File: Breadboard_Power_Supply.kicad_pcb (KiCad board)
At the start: 2 copper layers, 30 x 60 mm, 22 parts, among them J1 9V Battery, J2 USB_B, J3 Barrel_Jack_Switch, J4 1, J5 2, J6 3, SW1 SW_DIP_x03, U1 AMS1117-5.0, U2 AMS1117-3.3

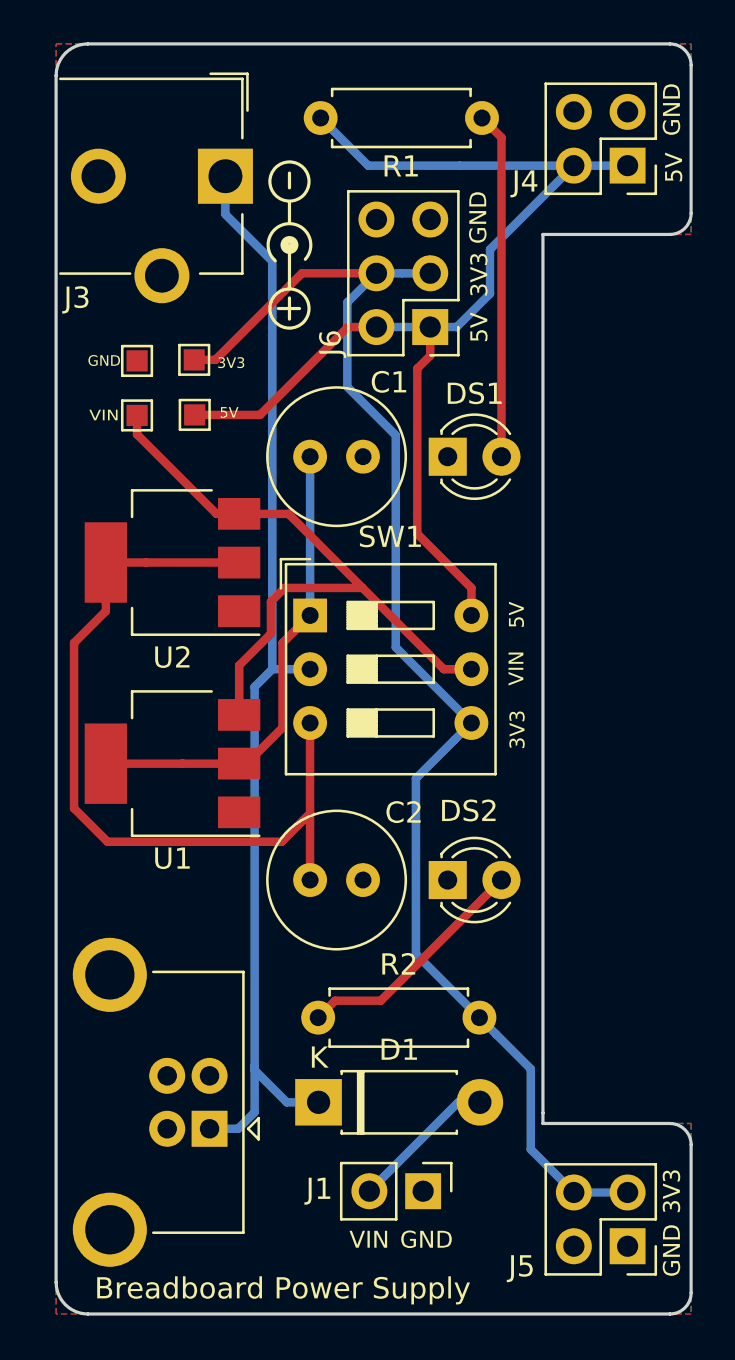
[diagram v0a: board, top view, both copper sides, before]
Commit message: Changed most footprints to SMD + Variable voltage
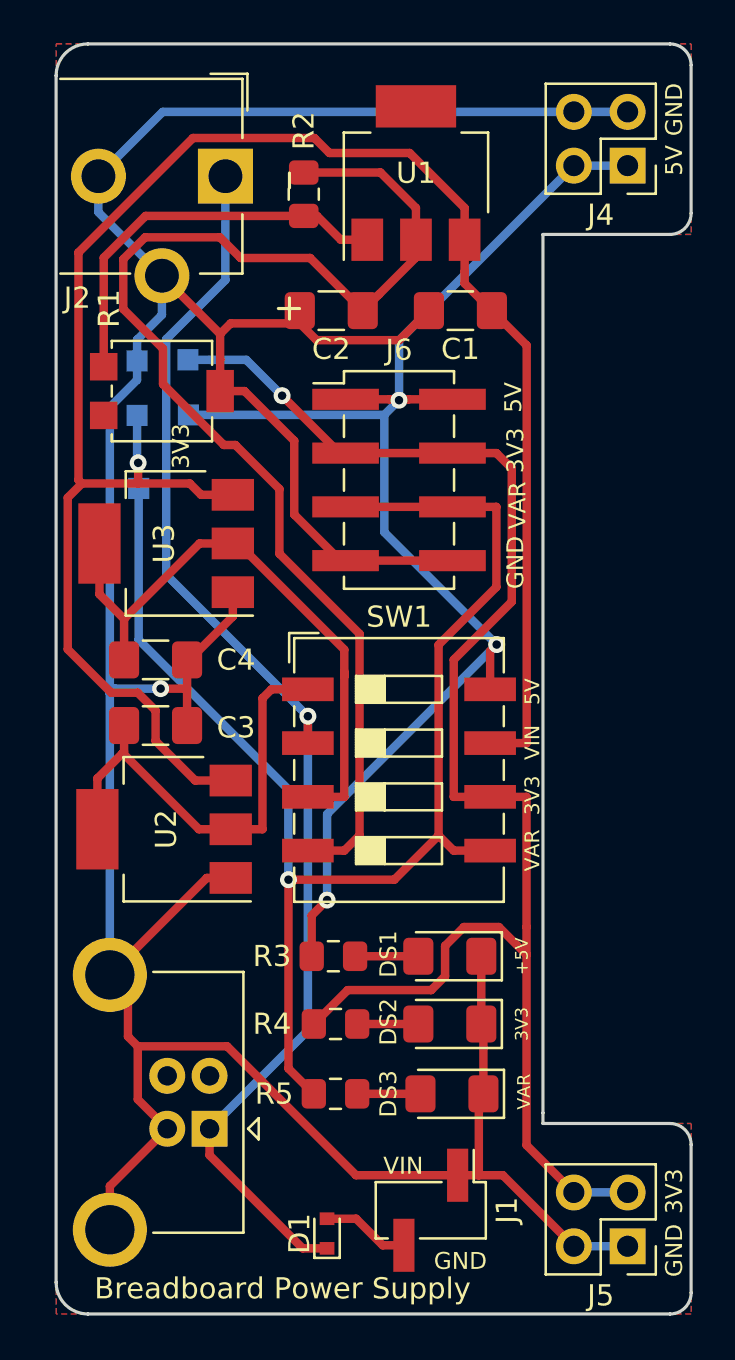
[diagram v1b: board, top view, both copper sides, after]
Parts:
- removed Polarity: Symbol_Barrel_Polarity, Symbol:Symbol_Barrel_Polarity
- removed REF**: OSHW-Logo2_7.3x6mm_SilkScreen, Symbol:OSHW-Logo2_7.3x6mm_SilkScreen
- added C1: 0.1uF, Capacitor_SMD:C_1206_3216Metric_Pad1.42x1.75mm_HandSolder, F.Cu at (151.6, 72.1)
- added C2: 1uF, Capacitor_SMD:C_1206_3216Metric_Pad1.42x1.75mm_HandSolder, F.Cu at (145.5, 72.1)
- added DS3: LED, LED_SMD:LED_1206_3216Metric_Pad1.42x1.75mm_HandSolder, F.Cu at (151.2, 109.1)
- added R1: 5k, Potentiometer_SMD:Potentiometer_Bourns_3314G_Vertical, F.Cu at (137.5, 75.9)
- added R2: 240R, Resistor_SMD:R_0805_2012Metric_Pad1.15x1.40mm_HandSolder, F.Cu at (144.2, 66.6)
- added R5: 820R, Resistor_SMD:R_0805_2012Metric_Pad1.15x1.40mm_HandSolder, F.Cu at (145.7, 109.1)
- added TP5: TestPoint, TestPoint:TestPoint_Pad_1.0x1.0mm, B.Cu at (136.4, 80.5)
- added U1: LM317_3PinPackage, Package_TO_SOT_SMD:SOT-223, F.Cu at (149.5, 65.6)
- C3: renamed from C1; footprint Capacitor_THT:C_Radial_D6.3mm_H11.0mm_P2.50mm -> Capacitor_SMD:C_1206_3216Metric_Pad1.42x1.75mm_HandSolder
- C4: renamed from C2; footprint Capacitor_THT:C_Radial_D6.3mm_H11.0mm_P2.50mm -> Capacitor_SMD:C_1206_3216Metric_Pad1.42x1.75mm_HandSolder
- D1: value 1N4007 -> 1N4148WT; footprint Diode_THT:D_DO-41_SOD81_P7.62mm_Horizontal -> Diode_SMD:D_SOD-523
- DS1, DS2: footprint LED_THT:LED_D3.0mm -> LED_SMD:LED_1206_3216Metric_Pad1.42x1.75mm_HandSolder
- J1: footprint Connector_PinHeader_2.54mm:PinHeader_1x02_P2.54mm_Vertical -> Connector_PinHeader_2.54mm:PinHeader_1x02_P2.54mm_Vertical_SMD_Pin1Left
- J6: value 3 -> Conn_02x04_Odd_Even; footprint Connector_PinHeader_2.54mm:PinHeader_2x03_P2.54mm_Vertical -> Connector_PinHeader_2.54mm:PinHeader_2x04_P2.54mm_Vertical_SMD
- R3: renamed from R1; footprint Resistor_THT:R_Axial_DIN0207_L6.3mm_D2.5mm_P7.62mm_Horizontal -> Resistor_SMD:R_0805_2012Metric_Pad1.15x1.40mm_HandSolder
- R4: renamed from R2; footprint Resistor_THT:R_Axial_DIN0207_L6.3mm_D2.5mm_P7.62mm_Horizontal -> Resistor_SMD:R_0805_2012Metric_Pad1.15x1.40mm_HandSolder
- SW1: value SW_DIP_x03 -> SW_DIP_x04; footprint Button_Switch_THT:SW_DIP_SPSTx03_Slide_9.78x9.8mm_W7.62mm_P2.54mm -> Button_Switch_SMD:SW_DIP_SPSTx04_Slide_9.78x12.34mm_W8.61mm_P2.54mm
- TP1: renamed from VIN; moved to B.Cu
- TP2: renamed from GND; moved to B.Cu
- TP3: renamed from  5V; moved to B.Cu
- TP4: renamed from 3V3; moved to B.Cu
- moved R3 39.6 mm to (145.6, 102.6)
- moved DS1 23.6 mm to (151.1, 102.6), turned to 180 degrees
- moved C3 14.6 mm to (137.2, 91.7)
- moved C4 12.7 mm to (137.2, 88.6)
- moved SW1 8.42 mm to (148.7, 93.8)
- moved J6 7.37 mm to (148.7, 80.1), turned to 0 degrees
- moved R4 6.81 mm to (145.7, 105.8), turned to 0 degrees
- moved DS2 6.80 mm to (151.1, 105.8), turned to 180 degrees
- moved D1 6.21 mm to (145.3, 115.7), turned to 90 degrees
- moved U2 3.13 mm to (137.6, 96.6)
- moved J1 0.97 mm to (150.2, 114.6)
- moved U3 0.95 mm to (137.7, 83.1)
- moved TP3 0.30 mm to (138.8, 77.0)
- moved TP4 0.30 mm to (138.7, 74.4)
- renumbered J3 to J2, J2 to J3, U1 to U2, U2 to U3
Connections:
- net 3.3V_OUT renamed /3.3V_OUT
- net 5V_OUT renamed /5V_OUT
- J3 pad 2: Net-(J2-Pad2) -> (no net)
- J3 pad 3: Net-(J2-Pad3) -> (no net)
- J3 pad 4: Net-(J2-Pad4) -> GND
- J6 pad 5: GND -> /VAR_VLG
- J6 pad 6: GND -> /VAR_VLG
- SW1 pad 4: +3V3 -> /VAR_VLG_OUT
- SW1 pad 5: VIN -> /VAR_VLG
- SW1 pad 6: +5V -> +3V3
- TP1 pad 1: VIN -> /VIN
- U2 pad 3: VIN -> /VIN
- U3 pad 3: VIN -> /VIN
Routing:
- net GND: track 0.00 -> 171.7 mm, vias 0 -> 1
- net /VIN: track 0.00 -> 90.9 mm, vias 0 -> 1
- net /VAR_VLG: track 0.00 -> 66.5 mm, vias 0 -> 1
- net /VAR_VLG_OUT: track 0.00 -> 60.0 mm
- net VIN: track 31.9 -> 0.00 mm
- net Net-(R1-Pad1): track 0.00 -> 18.9 mm
- net Net-(DS1-Pad2): track 16.4 -> 2.99 mm
- net +5V: track 54.4 -> 66.0 mm, vias 0 -> 3
- net /3.3V_OUT: track 40.2 -> 28.9 mm
- net Net-(DS2-Pad2): track 11.4 -> 2.89 mm
- net VDC: track 53.5 -> 60.7 mm, vias 0 -> 1
- net +3V3: track 66.0 -> 73.0 mm, vias 0 -> 1
- net Net-(DS3-Pad2): track 0.00 -> 2.99 mm
- net Net-(D1-Pad2): track 6.96 -> 4.15 mm
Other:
- net class Default: clearance 0.3 -> 0.1
- rule trace_clearance: 0.3 -> 0.1
- board text added: "+5V"
- board text added: "VAR"
- board text added: "VIN switch in the middle for simultaneous switching"

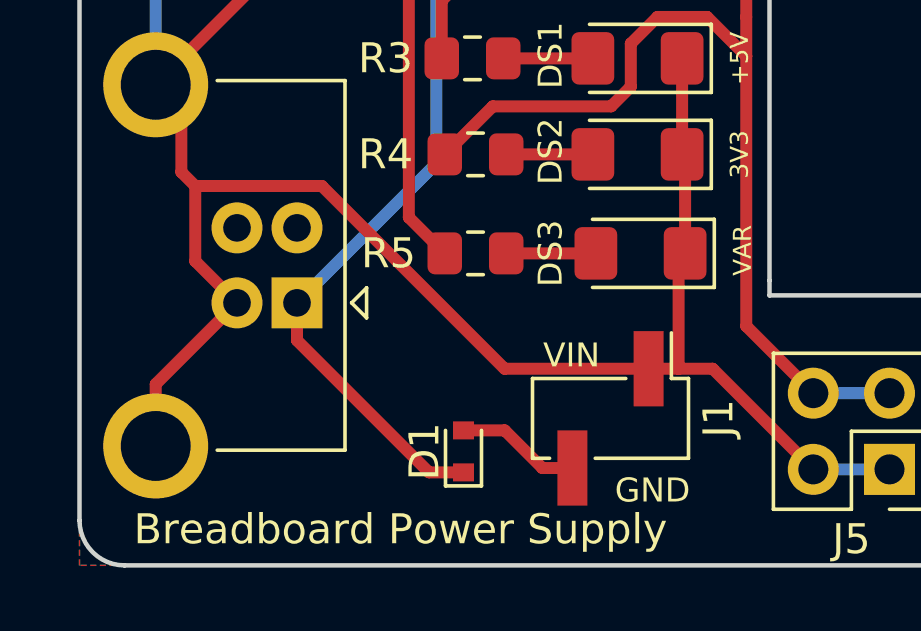
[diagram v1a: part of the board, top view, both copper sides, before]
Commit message: Protection diode changed + Datasheets
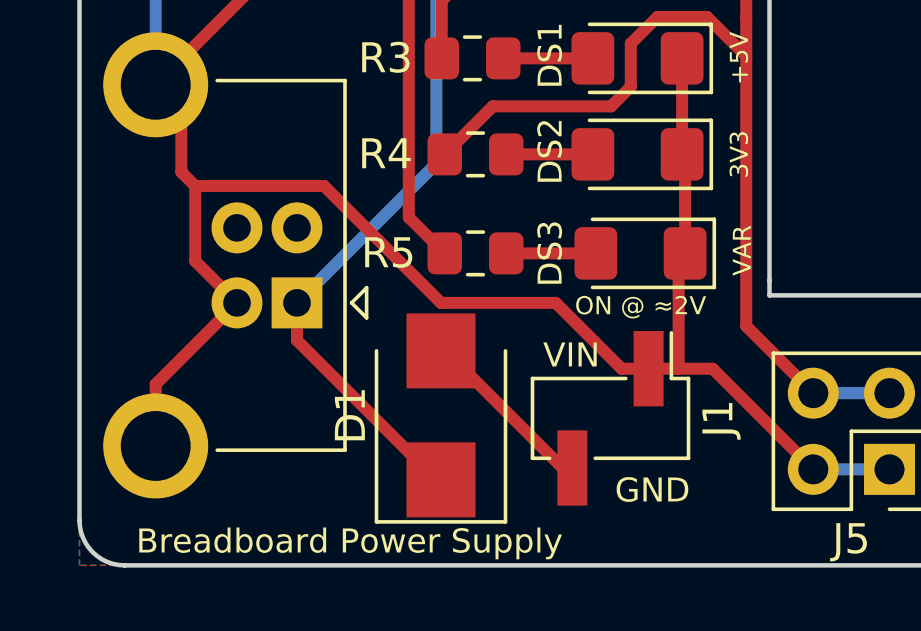
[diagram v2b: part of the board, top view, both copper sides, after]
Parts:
- D1: value 1N4148WT -> SS22T3G; footprint Diode_SMD:D_SOD-523 -> Diode_SMD:D_SMB
- moved D1 1.42 mm to (144.6, 114.5)
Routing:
- net Net-(D1-Pad2): track 4.15 -> 6.09 mm
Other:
- board text added: "ON @ ≈2V"
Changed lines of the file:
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@@
   (general
     (thickness 1.6)
-    (drawings 54)
-    (tracks 219)
+    (drawings 55)
+    (tracks 221)
     (zones 0)
     (modules 28)
@@
     (add_net "Net-(R1-Pad1)")
     (add_net VDC)
+  )
+  (module Diode_SMD:D_SMB (layer F.Cu)
+    (at 144.55 114.5 90)
+    (descr "Diode SMB (DO-214AA)")
+    (tags "Diode SMB (DO-214AA)")
+    (attr smd)
+    (fp_text reference D1 (at 0 -3 90) (layer F.SilkS)
+      (effects (font (size 1 1) (thickness 0.15)))
+    )
+    (fp_text value SS22T3G (at 0 3.1 90) (layer F.Fab)
+      (effects (font (size 1 1) (thickness 0.15)))
+    )
+    (fp_line (start -3.55 -2.15) (end 2.15 -2.15) (layer F.SilkS) (width 0.12))
+    (fp_line (start -3.55 2.15) (end 2.15 2.15) (layer F.SilkS) (width 0.12))
+    (fp_line (start -0.64944 0.00102) (end 0.50118 -0.79908) (layer F.Fab) (width 0.1))
+    (fp_line (start -0.64944 0.00102) (end 0.50118 0.75032) (layer F.Fab) (width 0.1))
+    (fp_line (start 0.50118 0.75032) (end 0.50118 -0.79908) (layer F.Fab) (width 0.1))
+    (fp_line (start -0.64944 -0.79908) (end -0.64944 0.80112) (layer F.Fab) (width 0.1))
+    (fp_line (start 0.50118 0.00102) (end 1.4994 0.00102) (layer F.Fab) (width 0.1))
+    (fp_line (start -0.64944 0.00102) (end -1.55114 0.00102) (layer F.Fab) (width 0.1))
+    (fp_line (start -3.65 2.25) (end -3.65 -2.25) (layer F.CrtYd) (width 0.05))
+    (fp_line (start 3.65 2.25) (end -3.65 2.25) (layer F.CrtYd) (width 0.05))
+    (fp_line (start 3.65 -2.25) (end 3.65 2.25) (layer F.CrtYd) (width 0.05))
+    (fp_line (start -3.65 -2.25) (end 3.65 -2.25) (layer F.CrtYd) (width 0.05))
+    (fp_line (start 2.3 -2) (end -2.3 -2) (layer F.Fab) (width 0.1))
+    (fp_line (start 2.3 -2) (end 2.3 2) (layer F.Fab) (width 0.1))
+    (fp_line (start -2.3 2) (end -2.3 -2) (layer F.Fab) (width 0.1))
+    (fp_line (start 2.3 2) (end -2.3 2) (layer F.Fab) (width 0.1))
+    (fp_line (start -3.55 -2.15) (end -3.55 2.15) (layer F.SilkS) (width 0.12))
+    (fp_text user %R (at 0 -3 90) (layer F.Fab)
+      (effects (font (size 1 1) (thickness 0.15)))
+    )
+    (pad 2 smd rect (at 2.15 0 90) (size 2.5 2.3) (layers F.Cu F.Paste F.Mask)
+      (net 7 "Net-(D1-Pad2)"))
+    (pad 1 smd rect (at -2.15 0 90) (size 2.5 2.3) (layers F.Cu F.Paste F.Mask)
+      (net 2 VDC))
+    (model ${KISYS3DMOD}/Diode_SMD.3dshapes/D_SMB.wrl
+      (at (xyz 0 0 0))
+      (scale (xyz 1 1 1))
+      (rotate (xyz 0 0 0))
+    )
   )
   (module Potentiometer_SMD:Potentiometer_Bourns_3314G_Vertical (layer F.Cu)
@@
     )
   )
-  (module Diode_SMD:D_SOD-523 (layer F.Cu)
-    (at 145.3 115.7 90)
-    (descr "http://www.diodes.com/datasheets/ap02001.pdf p.144")
-    (tags "Diode SOD523")
-    (attr smd)
-    (fp_text reference D1 (at 0 -1.3 90) (layer F.SilkS)
-      (effects (font (size 1 1) (thickness 0.15)))
-    )
-    (fp_text value 1N4148WT (at 0 1.4 90) (layer F.Fab)
-      (effects (font (size 1 1) (thickness 0.15)))
-    )
-    (fp_line (start 0.7 0.6) (end -1.15 0.6) (layer F.SilkS) (width 0.12))
-    (fp_line (start 0.7 -0.6) (end -1.15 -0.6) (layer F.SilkS) (width 0.12))
-    (fp_line (start 0.65 0.45) (end -0.65 0.45) (layer F.Fab) (width 0.1))
-    (fp_line (start -0.65 0.45) (end -0.65 -0.45) (layer F.Fab) (width 0.1))
-    (fp_line (start -0.65 -0.45) (end 0.65 -0.45) (layer F.Fab) (width 0.1))
-    (fp_line (start 0.65 -0.45) (end 0.65 0.45) (layer F.Fab) (width 0.1))
-    (fp_line (start -0.2 0.2) (end -0.2 -0.2) (layer F.Fab) (width 0.1))
-    (fp_line (start -0.2 0) (end -0.35 0) (layer F.Fab) (width 0.1))
-    (fp_line (start -0.2 0) (end 0.1 0.2) (layer F.Fab) (width 0.1))
-    (fp_line (start 0.1 0.2) (end 0.1 -0.2) (layer F.Fab) (width 0.1))
-    (fp_line (start 0.1 -0.2) (end -0.2 0) (layer F.Fab) (width 0.1))
-    (fp_line (start 0.1 0) (end 0.25 0) (layer F.Fab) (width 0.1))
-    (fp_line (start 1.25 0.7) (end -1.25 0.7) (layer F.CrtYd) (width 0.05))
-    (fp_line (start -1.25 0.7) (end -1.25 -0.7) (layer F.CrtYd) (width 0.05))
-    (fp_line (start -1.25 -0.7) (end 1.25 -0.7) (layer F.CrtYd) (width 0.05))
-    (fp_line (start 1.25 -0.7) (end 1.25 0.7) (layer F.CrtYd) (width 0.05))
-    (fp_line (start -1.15 -0.6) (end -1.15 0.6) (layer F.SilkS) (width 0.12))
-    (fp_text user %R (at 0 -1.3 90) (layer F.Fab)
-      (effects (font (size 1 1) (thickness 0.15)))
-    )
-    (pad 1 smd rect (at -0.7 0 270) (size 0.6 0.7) (layers F.Cu F.Paste F.Mask)
-      (net 2 VDC))
-    (pad 2 smd rect (at 0.7 0 270) (size 0.6 0.7) (layers F.Cu F.Paste F.Mask)
-      (net 7 "Net-(D1-Pad2)"))
-    (model ${KISYS3DMOD}/Diode_SMD.3dshapes/D_SOD-523.wrl
-      (at (xyz 0 0 0))
-      (scale (xyz 1 1 1))
-      (rotate (xyz 0 0 0))
-    )
-  )
   (module Capacitor_SMD:C_1206_3216Metric_Pad1.42x1.75mm_HandSolder (layer F.Cu)
     (at 137.2 88.6)
@@
     )
   )
+  (gr_text "ON @ ≈2V" (at 151.2 110.85) (layer F.SilkS)
+    (effects (font (size 0.6 0.6) (thickness 0.08)))
+  )
+  (gr_text "Breadboard Power Supply" (at 141.5 118.7) (layer F.SilkS)
+    (effects (font (size 0.8 0.8) (thickness 0.1)))
+  )
   (gr_text "VIN switch in the middle for simultaneous switching" (at 157.7 89.8 90) (layer Cmts.User)
     (effects (font (size 0.9 0.9) (thickness 0.1)))
@@
   (gr_text GND (at 151.6 117) (layer F.SilkS)
     (effects (font (size 0.8 0.8) (thickness 0.15)))
-  )
-  (gr_text "Breadboard Power Supply" (at 143.2 118.3) (layer F.SilkS)
-    (effects (font (size 1 1) (thickness 0.25)))
   )
   (gr_line (start 161 91) (end 161 115) (layer Dwgs.User) (width 0.15))
@@
   (segment (start 152.4703 112.945) (end 152.4703 109.3172) (width 0.4) (layer F.Cu) (net 1))
   (segment (start 152.4703 109.3172) (end 152.6875 109.1) (width 0.4) (layer F.Cu) (net 1))
-  (segment (start 136.3587 106.8542) (end 140.5798 106.8542) (width 0.4) (layer F.Cu) (net 1))
-  (segment (start 140.5798 106.8542) (end 146.6706 112.945) (width 0.4) (layer F.Cu) (net 1))
-  (segment (start 146.6706 112.945) (end 151.47 112.945) (width 0.4) (layer F.Cu) (net 1))
   (segment (start 136.325 74.475) (end 136.325 73.4747) (width 0.4) (layer B.Cu) (net 1))
   (segment (start 138.6875 91.7) (end 138.6875 89.958) (width 0.4) (layer F.Cu) (net 1))
@@
   (segment (start 135.04 76.66) (end 136.325 75.375) (width 0.4) (layer B.Cu) (net 1))
   (segment (start 135.04 90.2006) (end 135.04 76.66) (width 0.4) (layer B.Cu) (net 1))
+  (segment (start 150.57 112.945) (end 151.47 112.945) (width 0.4) (layer F.Cu) (net 1))
+  (segment (start 148.375 110.75) (end 150.57 112.945) (width 0.4) (layer F.Cu) (net 1))
+  (segment (start 144.55 110.75) (end 148.375 110.75) (width 0.4) (layer F.Cu) (net 1))
+  (segment (start 136.3587 106.8542) (end 140.6542 106.8542) (width 0.4) (layer F.Cu) (net 1))
+  (segment (start 140.6542 106.8542) (end 144.55 110.75) (width 0.4) (layer F.Cu) (net 1))
   (segment (start 144.395 91.26) (end 137.7033 84.5683) (width 0.4) (layer B.Cu) (net 2))
   (segment (start 137.7033 84.5683) (end 137.7033 73.4495) (width 0.4) (layer B.Cu) (net 2))
@@
   (segment (start 149.6125 102.6) (end 146.625 102.6) (width 0.4) (layer F.Cu) (net 5))
   (segment (start 149.6125 105.8) (end 146.725 105.8) (width 0.4) (layer F.Cu) (net 6))
-  (segment (start 148.93 116.255) (end 147.9297 116.255) (width 0.4) (layer F.Cu) (net 7))
-  (segment (start 145.3 115) (end 146.6747 115) (width 0.4) (layer F.Cu) (net 7))
-  (segment (start 146.6747 115) (end 147.9297 116.255) (width 0.4) (layer F.Cu) (net 7))
+  (segment (start 148.605 116.255) (end 148.93 116.255) (width 0.4) (layer F.Cu) (net 7))
+  (segment (start 144.6 112.25) (end 148.605 116.255) (width 0.4) (layer F.Cu) (net 7))
+  (segment (start 144.6 112.15) (end 144.6 112.25) (width 0.4) (layer F.Cu) (net 7))
   (segment (start 136.3753 80.2657) (end 136.3753 79.2926) (width 0.4) (layer F.Cu) (net 8))
   (segment (start 136.325 77.05) (end 136.325 79.2423) (width 0.4) (layer B.Cu) (net 8))
